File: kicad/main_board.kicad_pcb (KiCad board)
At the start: 2 copper layers, 42 x 67 mm, 65 parts, among them J1 Conn_01x18, J2 Conn_01x18, J3 Conn_01x07, J4 Conn_01x07, J5 Conn_01x07, J6 Conn_01x07, J7 Conn_01x07, J8 TYPE-C-31-M-12, J9 TYPE-C-31-M-12, Q1 DMG2301L-7, Q2 DMG2301L-7, Q3 DMG2301L-7, Q4 DMG2301L-7, Q5 DMG2301L-7, SW1 Reset, SW2 Boot, U1 XC6220B331MR, U2 RP2040, U3 W25Q128JVS, U4 COS724, U5 COS724, U6 USBLC6-2SC6, U7 USBLC6-2SC6, Y1 Crystal_GND24

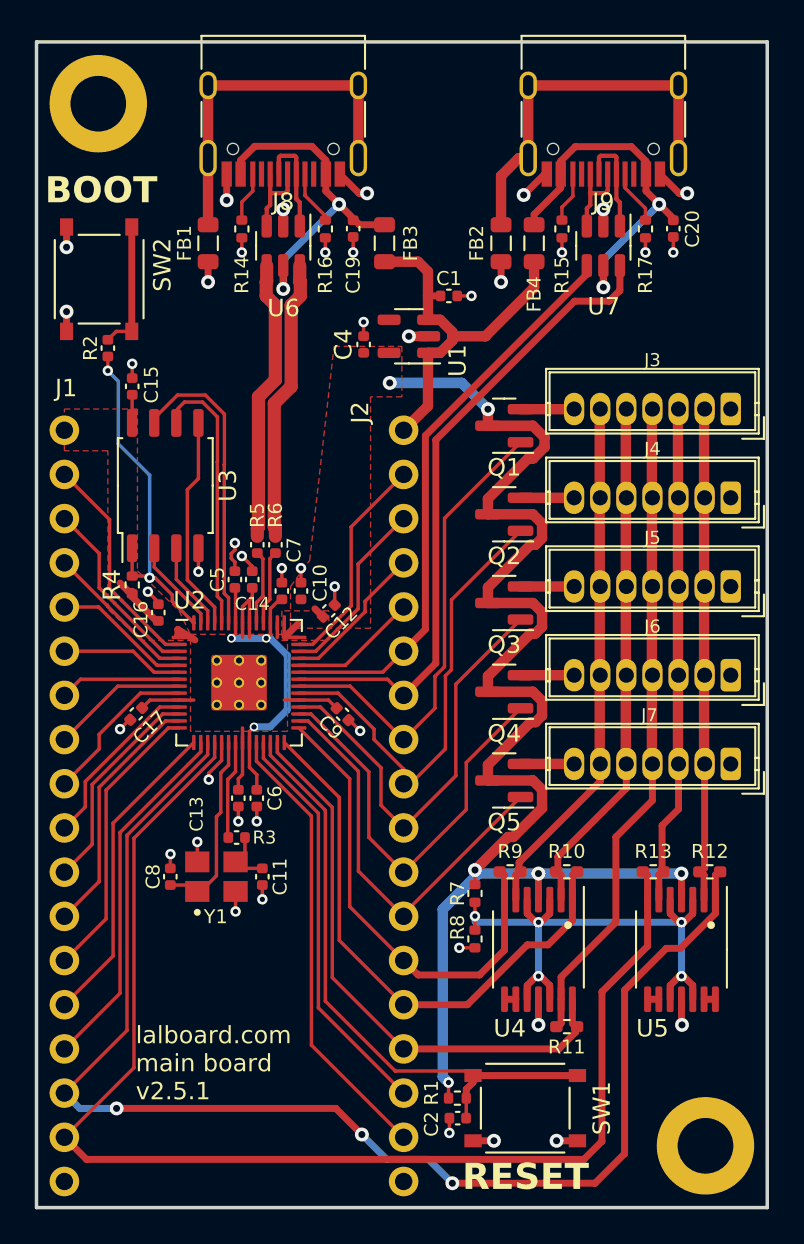
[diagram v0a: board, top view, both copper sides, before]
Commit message: Modifications to additional headers
- Added mouse header
- Added additional columns to support thumb through
- Switched to ribbon cables
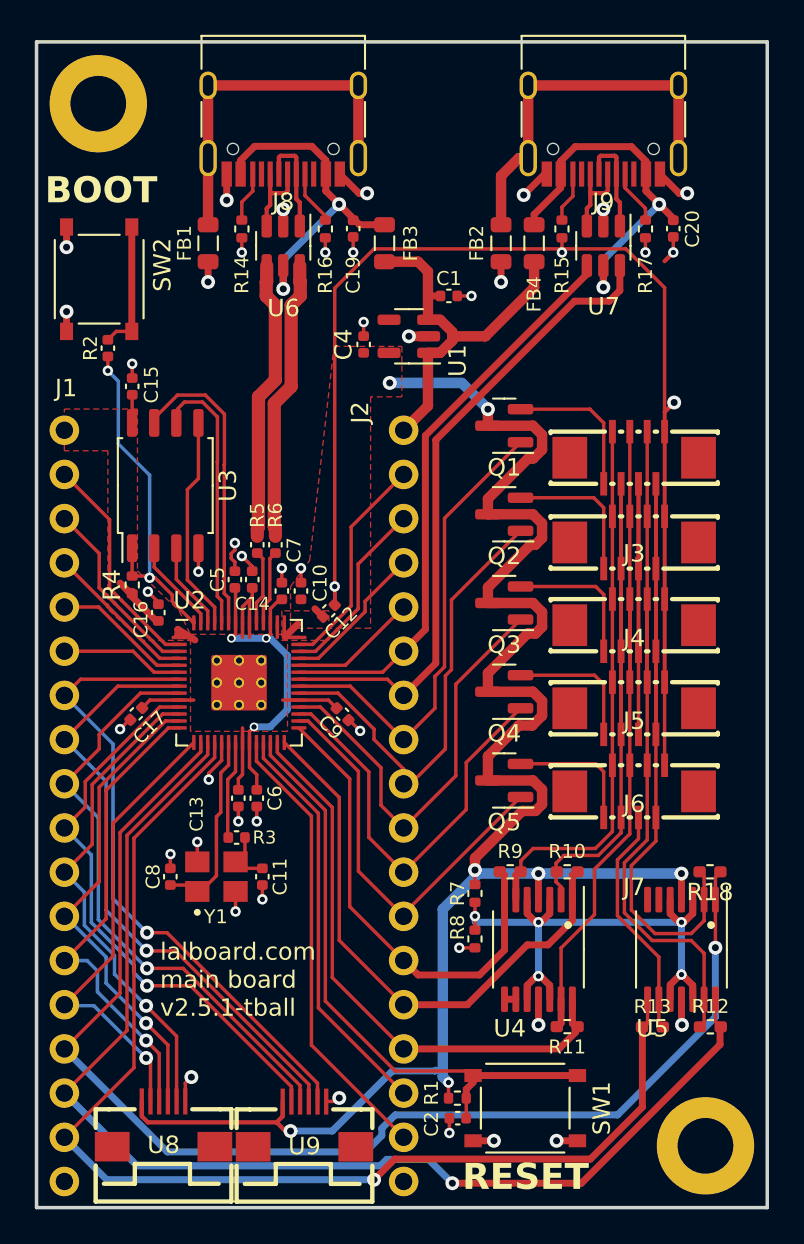
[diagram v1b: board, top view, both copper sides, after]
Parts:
- added R18: 2k, Resistor_SMD:R_0402_1005Metric_Pad0.72x0.64mm_HandSolder, F.Cu at (188.7, 80.7)
- added U8: FPC-0.5FX-6PWCR-H20, easyeda2kicad:FPC-SMD_6P-P0.50_FPC-0.5FX-6PWCR-H20, F.Cu at (157.3, 95.2)
- added U9: FPC-0.5FX-6PWCR-H20, easyeda2kicad:FPC-SMD_6P-P0.50_FPC-0.5FX-6PWCR-H20, F.Cu at (165.4, 95.2)
- J3, J4, J5, J6, J7: footprint lalboard:JST_ZH_B7B-ZR_1x07_P1.50mm_Vertical -> easyeda2kicad:FPC-SMD_8P-P0.50_AFC11-S08ICC-00
- moved R13 8.92 mm to (185.4, 89.6)
- moved R12 8.91 mm to (188.7, 89.6)
- moved J3 6.22 mm to (184.3, 56.9)
- moved J4 6.12 mm to (184.3, 61.8)
- moved J5 5.98 mm to (184.3, 66.5)
- moved J6 5.87 mm to (184.3, 71.3)
- moved J7 5.77 mm to (184.3, 76.1)
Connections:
- net /GPIO10 renamed /SCK1
- net /GPIO11 renamed /MOSI1
- net /GPIO12 renamed /SS1
- net /GPIO5 renamed /MISO2
- net /GPIO6 renamed /SCK2
- net /GPIO7 renamed /MOSI2
- net /GPIO8 renamed /SS2
- net /GPIO9 renamed /MISO1
- J1 pad 15: /GPIO13 -> /COL6_AMP
- J3 pad 2: /COL5 -> /COL6
- J3 pad 3: /COL4 -> /COL5
- J3 pad 4: /COL3 -> /COL4
- J3 pad 5: /COL2 -> /COL3
- J3 pad 6: /COL1 -> /COL2
- J3 pad 7: Net-(J3-Pin_7) -> /COL1
- J4 pad 2: /COL5 -> /COL6
- J4 pad 3: /COL4 -> /COL5
- J4 pad 4: /COL3 -> /COL4
- J4 pad 5: /COL2 -> /COL3
- J4 pad 6: /COL1 -> /COL2
- J4 pad 7: Net-(J4-Pin_7) -> /COL1
- J5 pad 2: /COL5 -> /COL6
- J5 pad 3: /COL4 -> /COL5
- J5 pad 4: /COL3 -> /COL4
- J5 pad 5: /COL2 -> /COL3
- J5 pad 6: /COL1 -> /COL2
- J5 pad 7: Net-(J5-Pin_7) -> /COL1
- J6 pad 2: /COL5 -> /COL6
- J6 pad 3: /COL4 -> /COL5
- J6 pad 4: /COL3 -> /COL4
- J6 pad 5: /COL2 -> /COL3
- J6 pad 6: /COL1 -> /COL2
- J6 pad 7: Net-(J6-Pin_7) -> /COL1
- J7 pad 2: /COL5 -> /COL6
- J7 pad 3: /COL4 -> /COL5
- J7 pad 4: /COL3 -> /COL4
- J7 pad 5: /COL2 -> /COL3
- J7 pad 6: /COL1 -> /COL2
- J7 pad 7: Net-(J7-Pin_7) -> /COL1
- Q1 pad 2: Net-(J3-Pin_7) -> Net-(J3-Pin_8)
- Q2 pad 2: Net-(J4-Pin_7) -> Net-(J4-Pin_8)
- Q3 pad 2: Net-(J5-Pin_7) -> Net-(J5-Pin_8)
- Q4 pad 2: Net-(J6-Pin_7) -> Net-(J6-Pin_8)
- Q5 pad 2: Net-(J7-Pin_7) -> Net-(J7-Pin_8)
- U2 pad 16: /GPIO13 -> /COL6_AMP
- U5 pad 1: /COL5_AMP -> /COL6_AMP
- U5 pad 13: Net-(U5D--) -> /COL5
- U5 pad 14: Net-(U5D--) -> /COL5_AMP
- U5 pad 2: /COL5 -> /COL6
- U5 pad 6: /COL4 -> Net-(U5B--)
- U5 pad 7: /COL4_AMP -> Net-(U5B--)
- U5 pad 8: Net-(U5C--) -> /COL4_AMP
- U5 pad 9: Net-(U5C--) -> /COL4
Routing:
- net GND: track 49.5 -> 135.4 mm, vias 42 -> 45
- net /COL6_AMP: track 0.00 -> 72.6 mm, vias 0 -> 1
- net /COL6: track 0.00 -> 61.9 mm
- net /MISO2: track 6.99 -> 37.0 mm, vias 0 -> 1
- net /SCK2: track 7.87 -> 35.5 mm, vias 0 -> 1
- net /COL2: track 29.3 -> 55.6 mm
- net /MOSI2: track 9.25 -> 34.3 mm, vias 0 -> 1
- net /SS2: track 10.3 -> 32.9 mm, vias 0 -> 1
- net +3.3V: track 110.7 -> 133.2 mm, vias 6 -> 7
- net /GPIO13: track 20.9 -> 0.00 mm
- net /MISO1: track 12.4 -> 28.2 mm, vias 0 -> 1
- net /COL5: track 27.5 -> 42.8 mm
- net /COL4: track 27.8 -> 42.1 mm
- net /SCK1: track 14.4 -> 27.6 mm, vias 0 -> 1
- net /MOSI1: track 16.5 -> 27.7 mm, vias 0 -> 1
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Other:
- board text added: "lalboard.com main board v2.5.1-tball"
- board text removed: "lalboard.com main board v2.5.1"

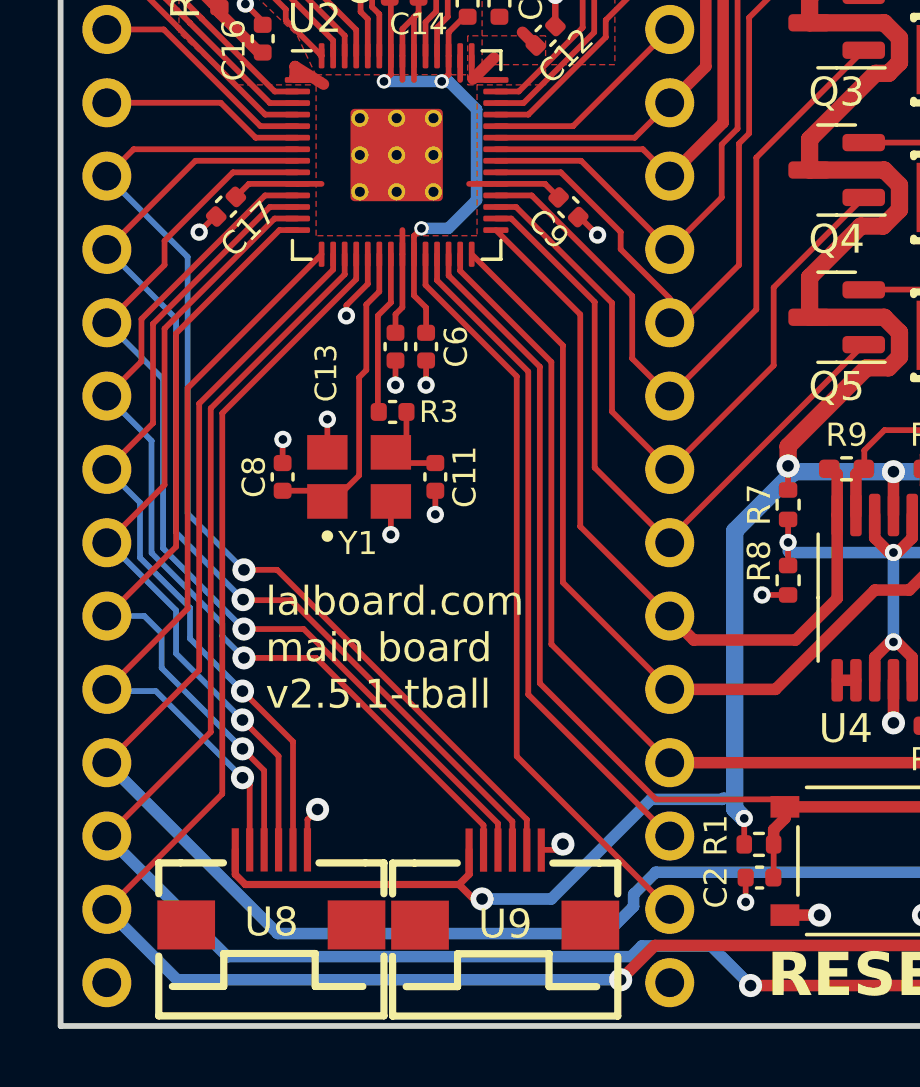
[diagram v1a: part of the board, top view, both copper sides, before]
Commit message: Single Trackball Correction
No need for two trackballs per side.
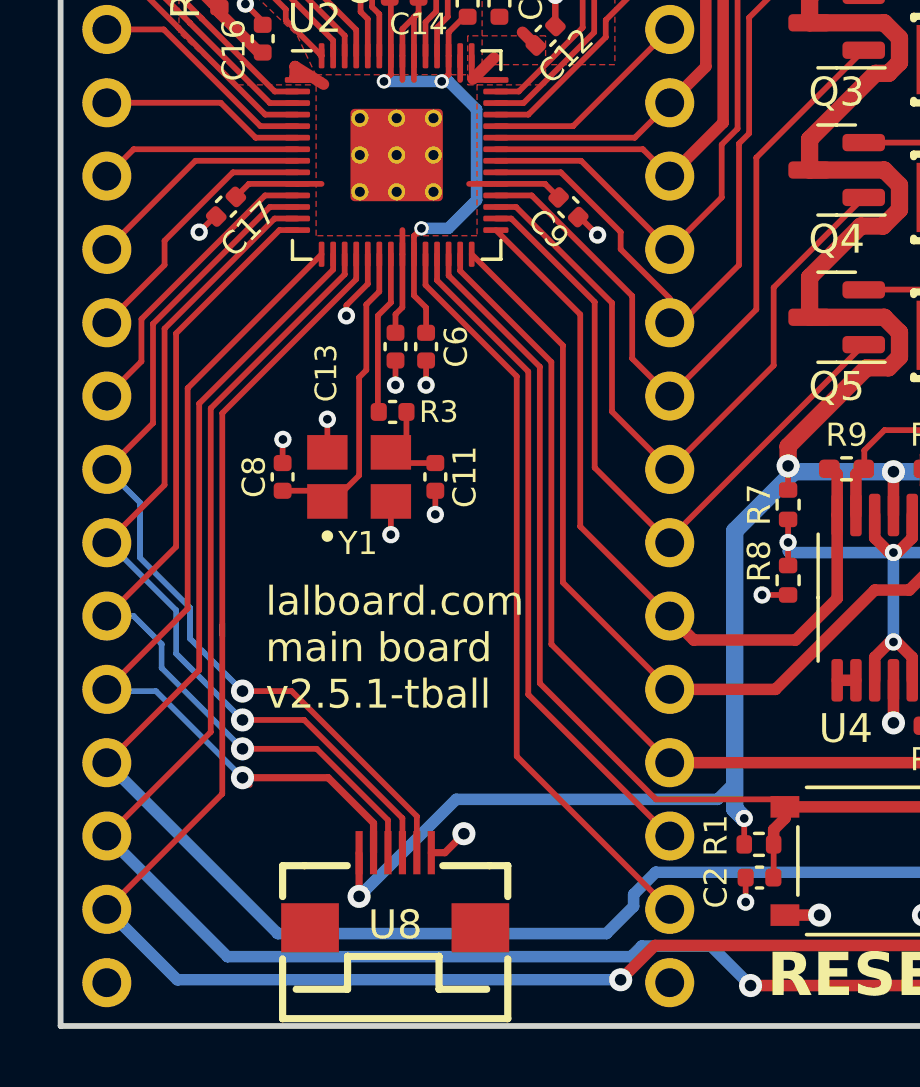
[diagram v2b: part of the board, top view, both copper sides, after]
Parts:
- removed U9: FPC-0.5FX-6PWCR-H20, easyeda2kicad:FPC-SMD_6P-P0.50_FPC-0.5FX-6PWCR-H20
- moved U8 4.29 mm to (161.6, 95.3)
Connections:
- net /MISO2 renamed /GPIO5
- net /MOSI2 renamed /GPIO7
- net /SCK2 renamed /GPIO6
- net /SS2 renamed /GPIO8
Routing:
- net /GPIO5: track 37.0 -> 6.99 mm, vias 1 -> 0
- net /GPIO6: track 35.5 -> 7.87 mm, vias 1 -> 0
- net /GPIO7: track 34.3 -> 9.25 mm, vias 1 -> 0
- net /GPIO8: track 32.9 -> 10.3 mm, vias 1 -> 0
- net +3.3V: track 133.2 -> 127.4 mm
- net /SS1: track 26.7 -> 30.7 mm
- net /MOSI1: track 27.7 -> 30.9 mm
- net /SCK1: track 27.6 -> 30.7 mm
- net /MISO1: track 28.2 -> 31.1 mm
- net GND: track 135.4 -> 134.4 mm, vias 45 -> 44

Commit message: DRC Fixes
DRC Fixes
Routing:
- net /COL4: track 42.1 -> 46.9 mm
- net Net-(U5B--): track 0.00 -> 0.65 mm
